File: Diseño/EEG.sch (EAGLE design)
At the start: 41 parts, among them IC1 REF2033AIDDCT, IC2 MCP73831T-2ACI_OT, IC3 LP38692MP-3.3_NOPB, J1 USB3500-30-A-KIT, J2 SJ3-35083A-TR, J3 1769

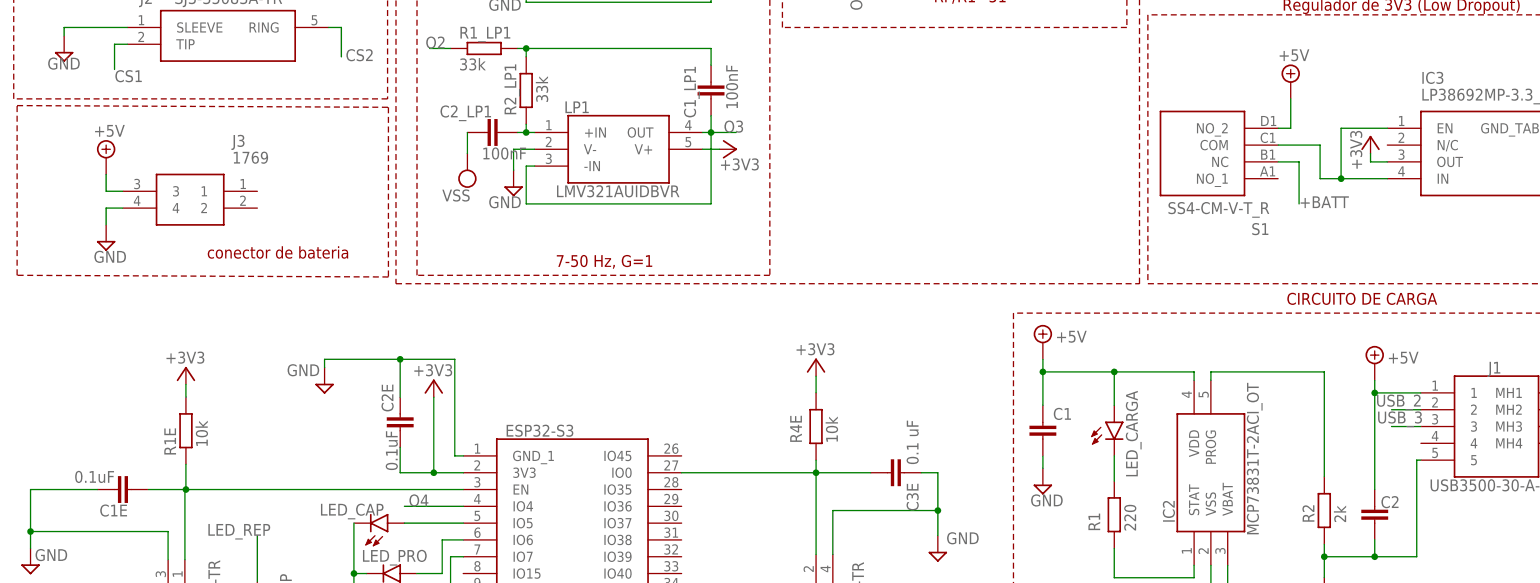
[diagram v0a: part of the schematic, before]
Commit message: enrutamiento y cambios en la conexion de bateria, Falta GND
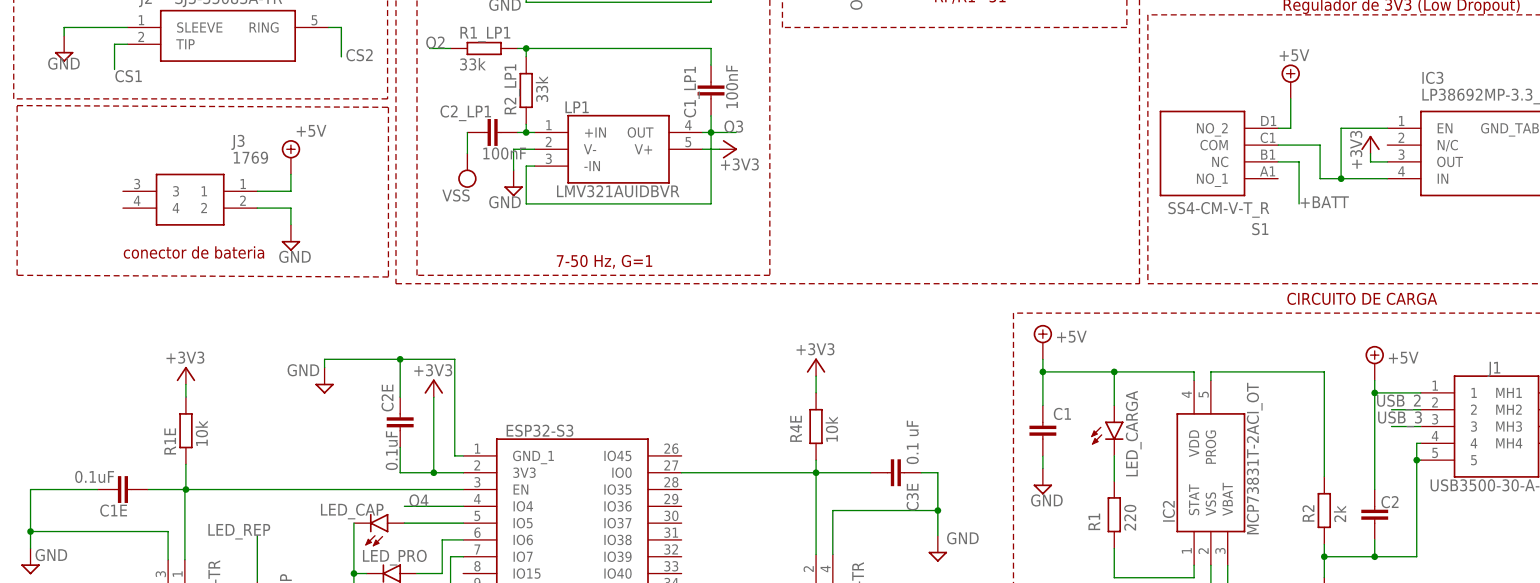
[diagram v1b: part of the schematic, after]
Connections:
- net +5V: now also J3.1; no longer J3.3
- net GND: now also J1.4, J3.2; no longer J3.4
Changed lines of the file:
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@@
 <wire x1="57.912" y1="103.886" x2="1.778" y2="104.14" width="0.1524" layer="94" style="shortdash"/>
 <wire x1="1.778" y1="104.14" x2="1.778" y2="129.794" width="0.1524" layer="94" style="shortdash"/>
-<text x="30.48" y="106.68" size="1.778" layer="94">conector de bateria</text>
+<text x="17.78" y="106.68" size="1.778" layer="94">conector de bateria</text>
 </plain>
 <instances>
@@
 <attribute name="VALUE" x="34.29" y="121.92" size="1.778" layer="96" align="center-left"/>
 </instance>
-<instance part="SUPPLY18" gate="+5V" x="15.24" y="121.92" smashed="yes">
-<attribute name="VALUE" x="13.335" y="125.095" size="1.778" layer="96"/>
-</instance>
-<instance part="SUPPLY19" gate="GND" x="15.24" y="109.22" smashed="yes">
-<attribute name="VALUE" x="13.335" y="106.045" size="1.778" layer="96"/>
+<instance part="SUPPLY18" gate="+5V" x="43.18" y="121.92" smashed="yes">
+<attribute name="VALUE" x="43.815" y="125.095" size="1.778" layer="96"/>
+</instance>
+<instance part="SUPPLY19" gate="GND" x="43.18" y="109.22" smashed="yes">
+<attribute name="VALUE" x="41.275" y="106.045" size="1.778" layer="96"/>
 </instance>
 </instances>
@@
 <pinref part="J1" gate="G$1" pin="5"/>
 <wire x1="213.36" y1="61.595" x2="207.01" y2="61.595" width="0.1524" layer="91"/>
+<wire x1="213.36" y1="76.2" x2="213.36" y2="61.595" width="0.1524" layer="91"/>
 <wire x1="213.995" y1="76.2" x2="213.36" y2="76.2" width="0.1524" layer="91"/>
-<wire x1="213.36" y1="76.2" x2="213.36" y2="61.595" width="0.1524" layer="91"/>
+<pinref part="J1" gate="G$1" pin="4"/>
+<wire x1="213.995" y1="78.74" x2="213.36" y2="78.74" width="0.1524" layer="91"/>
+<wire x1="213.36" y1="78.74" x2="213.36" y2="76.2" width="0.1524" layer="91"/>
+<junction x="213.36" y="76.2"/>
 </segment>
 <segment>
@@
 </segment>
 <segment>
+<pinref part="J3" gate="G$1" pin="2"/>
+<wire x1="38.1" y1="114.3" x2="43.18" y2="114.3" width="0.1524" layer="91"/>
 <pinref part="SUPPLY19" gate="GND" pin="GND"/>
-<wire x1="15.24" y1="111.76" x2="15.24" y2="114.3" width="0.1524" layer="91"/>
-<pinref part="J3" gate="G$1" pin="4"/>
-<wire x1="15.24" y1="114.3" x2="17.78" y2="114.3" width="0.1524" layer="91"/>
+<wire x1="43.18" y1="114.3" x2="43.18" y2="111.76" width="0.1524" layer="91"/>
 </segment>
 </net>
@@
 <segment>
 <pinref part="SUPPLY18" gate="+5V" pin="+5V"/>
-<pinref part="J3" gate="G$1" pin="3"/>
-<wire x1="15.24" y1="119.38" x2="15.24" y2="116.84" width="0.1524" layer="91"/>
-<wire x1="15.24" y1="116.84" x2="17.78" y2="116.84" width="0.1524" layer="91"/>
-</segment>
-</net>
+<wire x1="43.18" y1="119.38" x2="43.18" y2="116.84" width="0.1524" layer="91"/>
+<pinref part="J3" gate="G$1" pin="1"/>
+<wire x1="43.18" y1="116.84" x2="38.1" y2="116.84" width="0.1524" layer="91"/>
+</segment>
+</net>

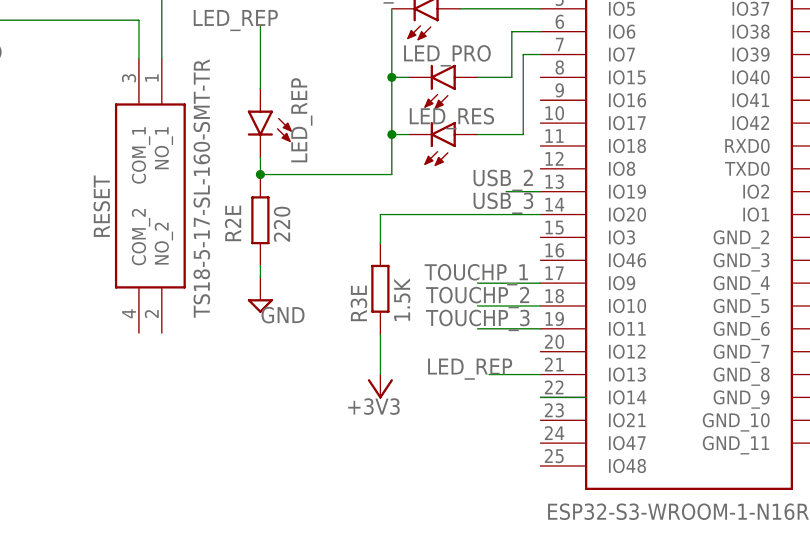
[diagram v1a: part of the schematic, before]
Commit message: Corrección Esp-32
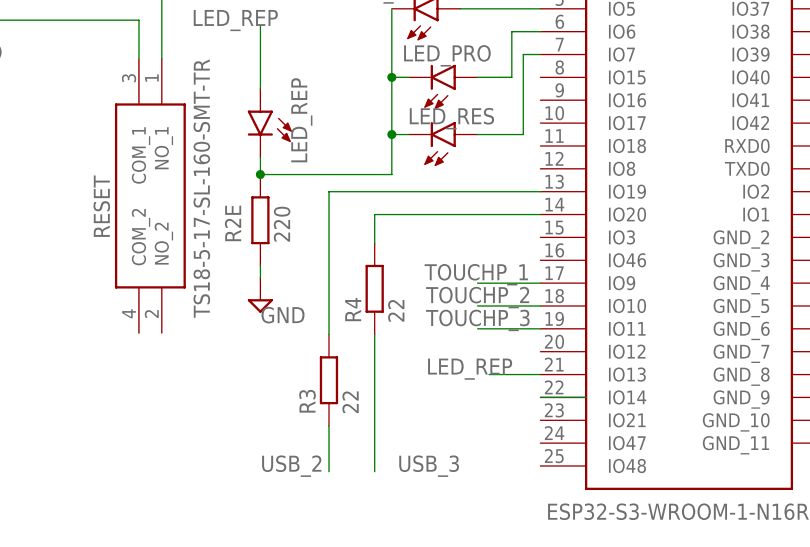
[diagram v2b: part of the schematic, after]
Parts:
- removed R3E: 1.5K, rcl:R-EU_R0805
- added R3, R4: 22, rcl:R-EU_R0805
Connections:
- new net N$14: ESP32-S3.IO20, R4.2
- new net N$18: ESP32-S3.IO19, R3.2
- net +3V3: no longer R3E.1
- net USB_2: now also R3.1; no longer ESP32-S3.IO19
- net USB_3: now also R4.1; no longer ESP32-S3.IO20, R3E.2
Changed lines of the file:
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@@
 <part name="SUPPLY16" library="supply2" library_urn="urn:adsk.eagle:library:372" deviceset="+5V" device=""/>
 <part name="SUPPLY17" library="supply2" library_urn="urn:adsk.eagle:library:372" deviceset="+5V" device=""/>
-<part name="R3E" library="rcl" library_urn="urn:adsk.eagle:library:334" deviceset="R-EU_" device="R0805" package3d_urn="urn:adsk.eagle:package:23553/2" value="1.5K"/>
-<part name="+3V11" library="supply1" library_urn="urn:adsk.eagle:library:371" deviceset="+3V3" device=""/>
 <part name="LED_REP" library="led" library_urn="urn:adsk.eagle:library:259" deviceset="LED" device="CHIPLED_0805" package3d_urn="urn:adsk.eagle:package:15821/2"/>
 <part name="LED_CAP" library="led" library_urn="urn:adsk.eagle:library:259" deviceset="LED" device="CHIPLED_0805" package3d_urn="urn:adsk.eagle:package:15821/2"/>
@@
 <part name="SUPPLY18" library="supply2" library_urn="urn:adsk.eagle:library:372" deviceset="+5V" device=""/>
 <part name="SUPPLY19" library="supply2" library_urn="urn:adsk.eagle:library:372" deviceset="GND" device=""/>
+<part name="R3" library="rcl" library_urn="urn:adsk.eagle:library:334" deviceset="R-EU_" device="R0805" package3d_urn="urn:adsk.eagle:package:23553/2" value="22"/>
+<part name="R4" library="rcl" library_urn="urn:adsk.eagle:library:334" deviceset="R-EU_" device="R0805" package3d_urn="urn:adsk.eagle:package:23553/2" value="22"/>
 </parts>
 <sheets>
@@
 <attribute name="VALUE" x="208.915" y="90.805" size="1.778" layer="96"/>
 </instance>
-<instance part="R3E" gate="G$1" x="51.435" y="35.56" smashed="yes" rot="R90">
-<attribute name="NAME" x="49.9364" y="31.75" size="1.778" layer="95" rot="R90"/>
-<attribute name="VALUE" x="54.737" y="31.75" size="1.778" layer="96" rot="R90"/>
-</instance>
-<instance part="+3V11" gate="G$1" x="51.435" y="23.495" smashed="yes" rot="R180">
-<attribute name="VALUE" x="47.625" y="21.59" size="1.778" layer="96"/>
-</instance>
 <instance part="LED_REP" gate="G$1" x="38.1" y="55.245" smashed="yes" rot="MR0">
 <attribute name="NAME" x="41.529" y="49.403" size="1.778" layer="95" rot="MR90"/>
@@
 <instance part="SUPPLY19" gate="GND" x="43.18" y="109.22" smashed="yes">
 <attribute name="VALUE" x="41.275" y="106.045" size="1.778" layer="96"/>
+</instance>
+<instance part="R3" gate="G$1" x="45.72" y="25.4" smashed="yes" rot="R90">
+<attribute name="NAME" x="44.2214" y="21.59" size="1.778" layer="95" rot="R90"/>
+<attribute name="VALUE" x="49.022" y="21.59" size="1.778" layer="96" rot="R90"/>
+</instance>
+<instance part="R4" gate="G$1" x="50.8" y="35.56" smashed="yes" rot="R90">
+<attribute name="NAME" x="49.3014" y="31.75" size="1.778" layer="95" rot="R90"/>
+<attribute name="VALUE" x="54.102" y="31.75" size="1.778" layer="96" rot="R90"/>
 </instance>
 </instances>
@@
 <pinref part="+3V10" gate="G$1" pin="+3V3"/>
 <wire x1="105.41" y1="123.19" x2="107.95" y2="123.19" width="0.1524" layer="91"/>
-</segment>
-<segment>
-<pinref part="R3E" gate="G$1" pin="1"/>
-<pinref part="+3V11" gate="G$1" pin="+3V3"/>
-<wire x1="51.435" y1="30.48" x2="51.435" y2="26.035" width="0.1524" layer="91"/>
 </segment>
 <segment>
@@
 </segment>
 <segment>
-<pinref part="ESP32-S3" gate="G$1" pin="IO19"/>
-<wire x1="69.215" y1="46.355" x2="65.405" y2="46.355" width="0.1524" layer="91"/>
-<label x="61.595" y="46.99" size="1.778" layer="95"/>
+<pinref part="R3" gate="G$1" pin="1"/>
+<wire x1="45.72" y1="20.32" x2="45.72" y2="15.24" width="0.1524" layer="91"/>
+<label x="38.1" y="15.24" size="1.778" layer="95"/>
 </segment>
 </net>
@@
 </segment>
 <segment>
-<pinref part="ESP32-S3" gate="G$1" pin="IO20"/>
-<label x="61.595" y="44.45" size="1.778" layer="95"/>
-<pinref part="R3E" gate="G$1" pin="2"/>
-<wire x1="51.435" y1="40.64" x2="51.435" y2="43.815" width="0.1524" layer="91"/>
-<wire x1="51.435" y1="43.815" x2="69.215" y2="43.815" width="0.1524" layer="91"/>
+<pinref part="R4" gate="G$1" pin="1"/>
+<wire x1="50.8" y1="30.48" x2="50.8" y2="15.24" width="0.1524" layer="91"/>
+<label x="53.34" y="15.24" size="1.778" layer="95"/>
 </segment>
 </net>
@@
 </segment>
 </net>
+<net name="N$14" class="0">
+<segment>
+<pinref part="ESP32-S3" gate="G$1" pin="IO20"/>
+<pinref part="R4" gate="G$1" pin="2"/>
+<wire x1="69.215" y1="43.815" x2="50.8" y2="43.815" width="0.1524" layer="91"/>
+<wire x1="50.8" y1="43.815" x2="50.8" y2="40.64" width="0.1524" layer="91"/>
+</segment>
+</net>
+<net name="N$18" class="0">
+<segment>
+<pinref part="ESP32-S3" gate="G$1" pin="IO19"/>
+<pinref part="R3" gate="G$1" pin="2"/>
+<wire x1="69.215" y1="46.355" x2="45.72" y2="46.355" width="0.1524" layer="91"/>
+<wire x1="45.72" y1="46.355" x2="45.72" y2="30.48" width="0.1524" layer="91"/>
+</segment>
+</net>

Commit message: añadido valores cap de carga
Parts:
- C1, C2: value (none) -> 10u
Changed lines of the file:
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@@
 <part name="IC2" library="MCP73831T-2ACI_OT" deviceset="MCP73831T-2ACI_OT" device=""/>
 <part name="LED_CARGA" library="led" library_urn="urn:adsk.eagle:library:259" deviceset="LED" device="CHIPLED_0805" package3d_urn="urn:adsk.eagle:package:15821/2"/>
-<part name="C1" library="rcl" library_urn="urn:adsk.eagle:library:334" deviceset="C-EU" device="C0805K" package3d_urn="urn:adsk.eagle:package:23681/2"/>
-<part name="C2" library="rcl" library_urn="urn:adsk.eagle:library:334" deviceset="C-EU" device="C0805K" package3d_urn="urn:adsk.eagle:package:23681/2"/>
+<part name="C1" library="rcl" library_urn="urn:adsk.eagle:library:334" deviceset="C-EU" device="C0805K" package3d_urn="urn:adsk.eagle:package:23681/2" value="10u"/>
+<part name="C2" library="rcl" library_urn="urn:adsk.eagle:library:334" deviceset="C-EU" device="C0805K" package3d_urn="urn:adsk.eagle:package:23681/2" value="10u"/>
 <part name="R1" library="rcl" library_urn="urn:adsk.eagle:library:334" deviceset="R-EU_" device="R0805" package3d_urn="urn:adsk.eagle:package:23553/2" value="220"/>
 <part name="R2" library="rcl" library_urn="urn:adsk.eagle:library:334" deviceset="R-EU_" device="R0805" package3d_urn="urn:adsk.eagle:package:23553/2" value="2k"/>

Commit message: Correcciones del profesor
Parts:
- C1, C2: value 10u -> (none)
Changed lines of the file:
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@@
 <part name="IC2" library="MCP73831T-2ACI_OT" deviceset="MCP73831T-2ACI_OT" device=""/>
 <part name="LED_CARGA" library="led" library_urn="urn:adsk.eagle:library:259" deviceset="LED" device="CHIPLED_0805" package3d_urn="urn:adsk.eagle:package:15821/2"/>
-<part name="C1" library="rcl" library_urn="urn:adsk.eagle:library:334" deviceset="C-EU" device="C0805K" package3d_urn="urn:adsk.eagle:package:23681/2" value="10u"/>
-<part name="C2" library="rcl" library_urn="urn:adsk.eagle:library:334" deviceset="C-EU" device="C0805K" package3d_urn="urn:adsk.eagle:package:23681/2" value="10u"/>
+<part name="C1" library="rcl" library_urn="urn:adsk.eagle:library:334" deviceset="C-EU" device="C0805K" package3d_urn="urn:adsk.eagle:package:23681/2"/>
+<part name="C2" library="rcl" library_urn="urn:adsk.eagle:library:334" deviceset="C-EU" device="C0805K" package3d_urn="urn:adsk.eagle:package:23681/2"/>
 <part name="R1" library="rcl" library_urn="urn:adsk.eagle:library:334" deviceset="R-EU_" device="R0805" package3d_urn="urn:adsk.eagle:package:23553/2" value="220"/>
 <part name="R2" library="rcl" library_urn="urn:adsk.eagle:library:334" deviceset="R-EU_" device="R0805" package3d_urn="urn:adsk.eagle:package:23553/2" value="2k"/>
@@
 <attribute name="VALUE" x="237.49" y="71.12" size="1.778" layer="96"/>
 </instance>
-<instance part="GND6" gate="GND" x="8.89" y="137.795" smashed="yes">
-<attribute name="VALUE" x="6.35" y="135.255" size="1.778" layer="96"/>
+<instance part="GND6" gate="GND" x="-19.05" y="137.795" smashed="yes">
+<attribute name="VALUE" x="-21.59" y="135.255" size="1.778" layer="96"/>
 </instance>
 <instance part="C3E" gate="G$1" x="135.89" y="74.295" smashed="yes" rot="R270">
@@
 <attribute name="VALUE" x="34.29" y="121.92" size="1.778" layer="96" align="center-left"/>
 </instance>
-<instance part="SUPPLY18" gate="+5V" x="43.18" y="121.92" smashed="yes">
-<attribute name="VALUE" x="43.815" y="125.095" size="1.778" layer="96"/>
+<instance part="SUPPLY18" gate="+5V" x="-10.16" y="127" smashed="yes">
+<attribute name="VALUE" x="-9.525" y="130.175" size="1.778" layer="96"/>
 </instance>
 <instance part="SUPPLY19" gate="GND" x="43.18" y="109.22" smashed="yes">
@@
 <segment>
 <pinref part="GND6" gate="GND" pin="GND"/>
-<wire x1="8.89" y1="141.605" x2="8.89" y2="140.335" width="0.1524" layer="91"/>
+<wire x1="8.89" y1="141.605" x2="-19.05" y2="140.335" width="0.1524" layer="91"/>
 <pinref part="J2" gate="G$1" pin="SLEEVE"/>
 <wire x1="18.415" y1="141.605" x2="8.89" y2="141.605" width="0.1524" layer="91"/>
@@
 <segment>
 <pinref part="SUPPLY18" gate="+5V" pin="+5V"/>
-<wire x1="43.18" y1="119.38" x2="43.18" y2="116.84" width="0.1524" layer="91"/>
+<wire x1="-10.16" y1="124.46" x2="43.18" y2="116.84" width="0.1524" layer="91"/>
 <pinref part="J3" gate="G$1" pin="1"/>
 <wire x1="43.18" y1="116.84" x2="38.1" y2="116.84" width="0.1524" layer="91"/>
@@
 <net name="+5V1" class="0">
 <segment>
-<wire x1="74.295" y1="23.495" x2="69.215" y2="23.495" width="0.1524" layer="91"/>
+<wire x1="64.135" y1="23.495" x2="69.215" y2="23.495" width="0.1524" layer="91"/>
 <pinref part="ESP32-S3" gate="G$1" pin="IO14"/>
 </segment>
